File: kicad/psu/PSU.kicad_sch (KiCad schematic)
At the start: 54 parts, among them J1 B2B-PH-K-S, J3 UJ20-C-H-G-SMT-1-P16-TR, U1 BQ21040DBVR, U2 RT4812GJ8F, U3 AP3445LW6-7, U4 Connector MCU, U5 LM66200DRLR, U6 TLV75733PDBVR, U7 Connector Sensor

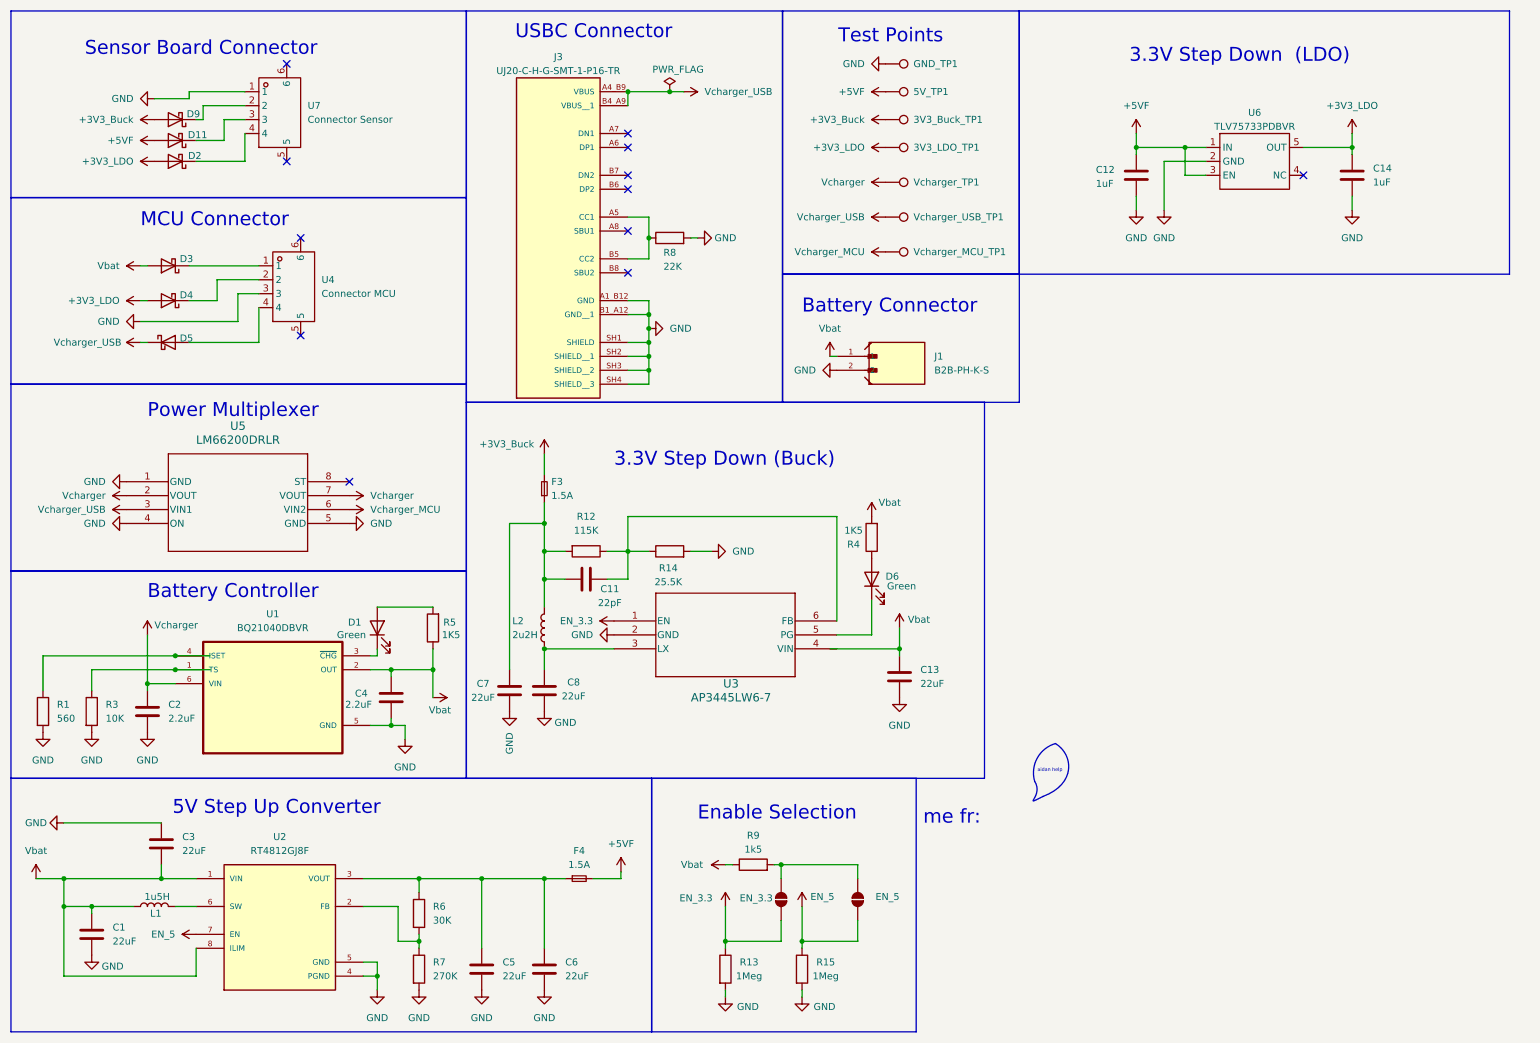
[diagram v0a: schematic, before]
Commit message: feat: basically complete the psu board
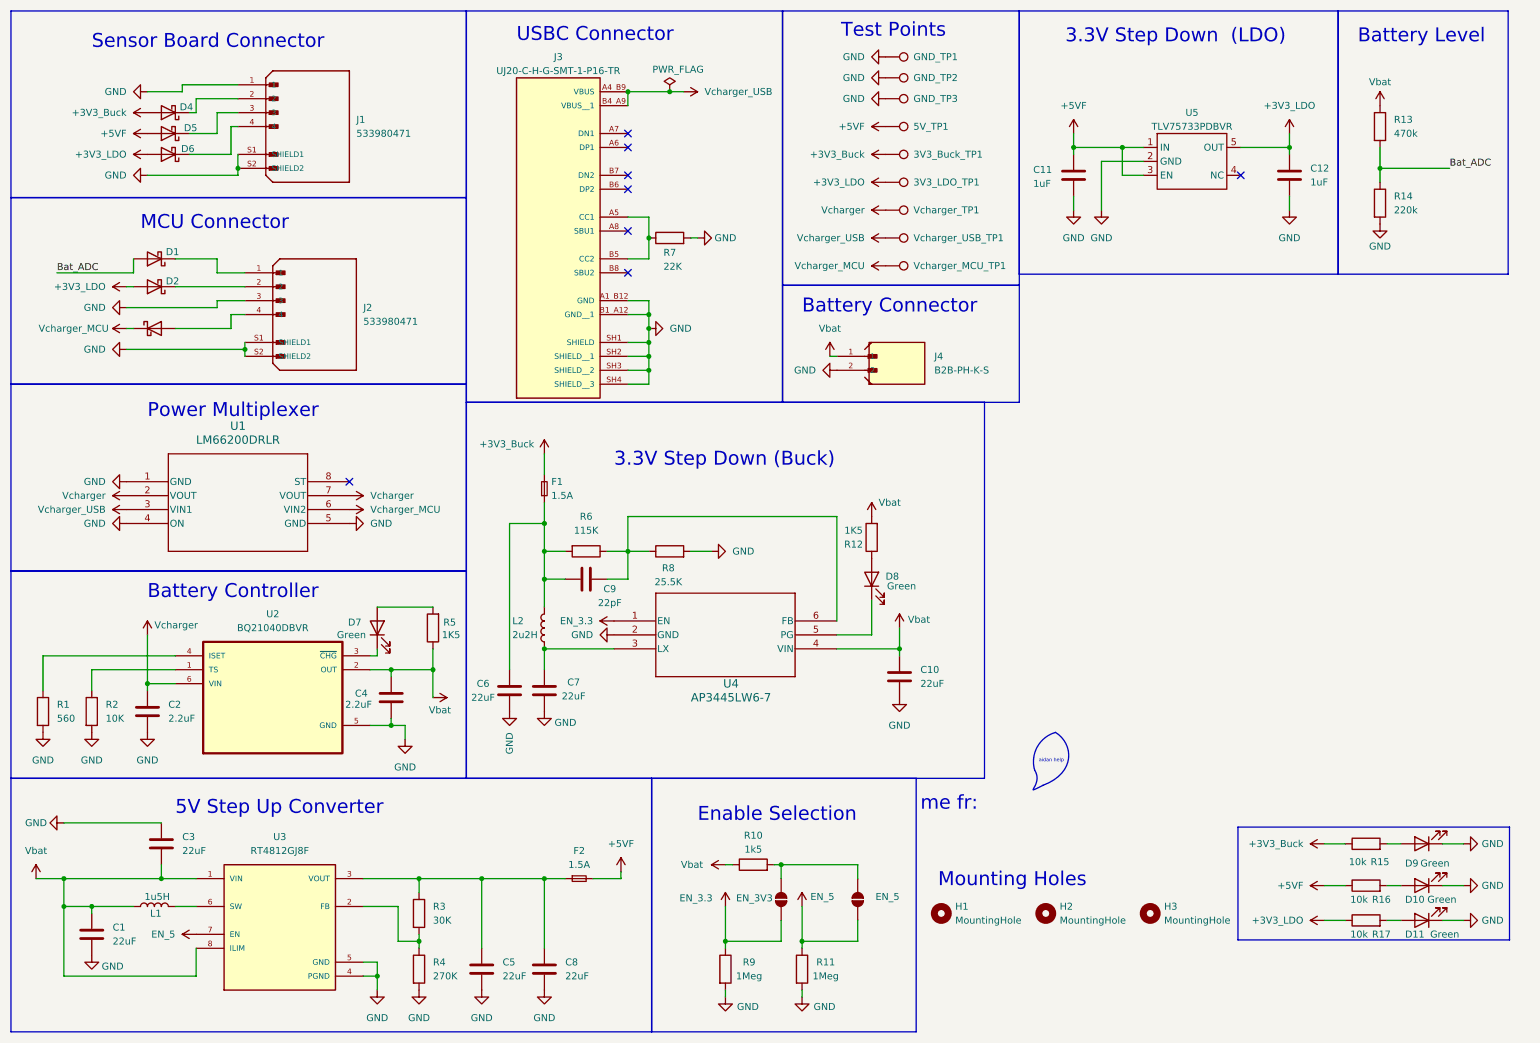
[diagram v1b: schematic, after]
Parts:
- removed U4: Connector MCU, ProLib_pcs_2026-01-27:CONN-SMD_4P-P1.25-MX1.25-4P-WT, symbol PSAT_Library:ZX-MX1.25-4PWT
- removed U7: Connector Sensor, ProLib_pcs_2026-01-27:CONN-SMD_4P-P1.25-MX1.25-4P-WT, symbol PSAT_Library:ZX-MX1.25-4PWT
- added D10, D11, D9: Green, LED_SMD:LED_0805_2012Metric, symbol Device:LED
- added GND_TP2, GND_TP3: TestPoint, TestPoint:TestPoint_Pad_1.5x1.5mm, symbol Connector:TestPoint
- added H1, H2, H3: MountingHole, MountingHole:MountingHole_3mm_Pad, symbol Mechanical:MountingHole
- added J1, J2: 533980471, PSAT_Library:MOLEX_533980471, symbol PSAT_Library:533980471
- added R13: 470k, Resistor_SMD:R_0805_2012Metric, symbol Device:R
- added R14: 220k, Resistor_SMD:R_0805_2012Metric, symbol Device:R
- added R15, R16, R17: 10k, Resistor_SMD:R_0805_2012Metric, symbol Device:R
- C11: renamed from C12; footprint (none) -> Capacitor_SMD:C_0805_2012Metric
- C12: renamed from C14; footprint (none) -> Capacitor_SMD:C_0805_2012Metric
- F1: renamed from F3; footprint Fuses:0451Series_LTF -> PSAT_Library:FUS_VISHAY_MFU0805_VIS
- F2: renamed from F4; footprint Fuses:0451Series_LTF -> PSAT_Library:FUS_VISHAY_MFU0805_VIS
- J3: footprint SAMESKY_UJ20-C-H-G-SMT-1-P16-TR -> PSAT_Library:SAMESKY_UJ20-C-H-G-SMT-P16-TR
- U1: renamed from U5; footprint footprints:SOT-5X3_DRL_TEX -> PSAT_Library:SOT-5X3_DRL_TEX
- U5: renamed from U6; footprint TLV75733PDBVR:SOT-23-5_L2.9-W1.6-P0.95-LS2.8-BL -> PSAT_Library:SOT95P280X145-5N
- renumbered C13 to C10, C7 to C6, C8 to C7, C6 to C8, C11 to C9, D3 to D1, D4 to D2, D5 to D3, D9 to D4, D11 to D5, D2 to D6, D1 to D7, D6 to D8, EN_3.3 to EN_3V3, J1 to J4, R9 to R10, R15 to R11, R4 to R12, R3 to R2, R6 to R3, R7 to R4, R12 to R6, R8 to R7, R14 to R8, R13 to R9, U1 to U2, U2 to U3, U3 to U4
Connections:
- net +3V3_Buck: now also R15.1
- net +3V3_LDO: now also R17.1
- net +5VF: now also R16.1
- net GND: now also D10.1 (K), D11.1 (K), D9.1 (K), GND_TP2.1, GND_TP3.1, J1.1, J1.S1 (SHIELD1), J1.S2 (SHIELD2), J2.3, J2.S1 (SHIELD1), J2.S2 (SHIELD2), R14.2
- net Vbat: now also U4.4 (VIN), R13.1; no longer D1.2 (A)
- net Vcharger_MCU: now also D3.1 (K)
- net Vcharger_USB: no longer D3.1 (K)
- net at D2.1 (K): now also J2.2
- net at D6.1 (K): now also J1.4
- net at D5.1 (K): now also J1.3
- net at D4.1 (K): now also J1.2
- net at D3.2 (A): now also J2.4
- net at D1.1 (K): now also J2.1
- new net: D10.2 (A), R16.2
- new net: D11.2 (A), R17.2
- new net: D9.2 (A), R15.2
- new net Bat_ADC: D1.2 (A), R13.2, R14.1
- no-connect marks 12 -> 8
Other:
- note added: "Battery Level"
- note added: "Mounting Holes"
- moved on the sheet: 3V3_Buck_TP1, 3V3_LDO_TP1, 5V_TP1, C11, C12, D1, D2, D4, D5, D6, GND_TP1, U5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

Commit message: fix: all errors on the psu pcb
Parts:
- C2, C4: value 2.2uF -> 1uF
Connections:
- net +5VF: no longer C11.1, U5.1 (IN), U5.3 (EN)
- net Vbat: no longer C10.1, U4.4 (VIN)
- net +5VU: now reaches C5.2, C8.1, F2.1, R3.1, U3.3 (VOUT)
- net +5VU: now also C10.1, C11.1, U4.4 (VIN), U5.1 (IN), U5.3 (EN)
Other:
- moved on the sheet: J4
